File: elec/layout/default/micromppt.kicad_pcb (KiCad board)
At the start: 2 copper layers, 29 x 28.5 mm, 19 parts, among them J1 ?, J2 ?, U1 ?, U2 ?, U3 ?, U4 ?, U5 ?

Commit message: pcb update and actions retry
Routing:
- net gnd: vias 9 -> 21
- added copper zone on F.Cu, net gnd
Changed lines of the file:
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@@
 			(outputformat 1)
 			(mirror no)
-			(drillshape 1)
+			(drillshape 0)
 			(scaleselection 1)
-			(outputdirectory "")
+			(outputdirectory "../../../gerbers/")
 		)
 	)
@@
 	)
 	(gr_line
-		(start 87 39.2)
-		(end 72 39.2)
+		(start 65 67.75)
+		(end 94 67.75)
 		(stroke
 			(width 0.2)
@@
 	)
 	(gr_line
-		(start 65 67.75)
-		(end 94 67.75)
+		(start 87 39.2)
+		(end 72 39.2)
 		(stroke
 			(width 0.2)
@@
 	)
 	(segment
-		(start 86.1425 45.12)
-		(end 85.4 45.12)
-		(width 0.3048)
-		(layer "F.Cu")
-		(net 2)
-	)
-	(segment
 		(start 85.6 43.6)
 		(end 82.3 40.3)
@@
 	)
 	(segment
-		(start 85.6 44.92)
+		(start 85.6 44.5775)
 		(end 85.6 43.6)
 		(width 0.3048)
@@
 	)
 	(segment
+		(start 81.1525 44.25)
+		(end 80.2825 45.12)
+		(width 0.3048)
+		(layer "F.Cu")
+		(net 2)
+	)
+	(segment
 		(start 82.3 40.3)
 		(end 78.25 40.3)
@@
 	)
 	(segment
-		(start 74.76 41.64)
-		(end 74.76 42)
+		(start 85.2725 44.25)
+		(end 81.1525 44.25)
 		(width 0.3048)
 		(layer "F.Cu")
@@
 	(segment
 		(start 86.1425 45.12)
-		(end 80.2825 45.12)
+		(end 85.2725 44.25)
 		(width 0.3048)
 		(layer "F.Cu")
@@
 	)
 	(segment
-		(start 85.4 45.12)
-		(end 85.6 44.92)
+		(start 74.76 41.64)
+		(end 74.76 42)
+		(width 0.3048)
+		(layer "F.Cu")
+		(net 2)
+	)
+	(segment
+		(start 86.1425 45.12)
+		(end 85.6 44.5775)
 		(width 0.3048)
 		(layer "F.Cu")
@@
 	)
 	(via
+		(at 68 45.25)
+		(size 0.8)
+		(drill 0.4)
+		(layers "F.Cu" "B.Cu")
+		(free yes)
+		(net 6)
+	)
+	(via
+		(at 76.75 47.5)
+		(size 0.8)
+		(drill 0.4)
+		(layers "F.Cu" "B.Cu")
+		(free yes)
+		(net 6)
+	)
+	(via
+		(at 78.5 45.25)
+		(size 0.8)
+		(drill 0.4)
+		(layers "F.Cu" "B.Cu")
+		(free yes)
+		(net 6)
+	)
+	(via
 		(at 76.55 51)
 		(size 0.8)
@@
 	)
 	(via
+		(at 87.75 50.75)
+		(size 0.8)
+		(drill 0.4)
+		(layers "F.Cu" "B.Cu")
+		(free yes)
+		(net 6)
+	)
+	(via
+		(at 81.75 43.5)
+		(size 0.8)
+		(drill 0.4)
+		(layers "F.Cu" "B.Cu")
+		(free yes)
+		(net 6)
+	)
+	(via
 		(at 81.9 57.6)
 		(size 0.8)
@@
 	)
 	(via
+		(at 77.5 51.5)
+		(size 0.8)
+		(drill 0.4)
+		(layers "F.Cu" "B.Cu")
+		(free yes)
+		(net 6)
+	)
+	(via
+		(at 68 48.75)
+		(size 0.8)
+		(drill 0.4)
+		(layers "F.Cu" "B.Cu")
+		(free yes)
+		(net 6)
+	)
+	(via
+		(at 68 50.5)
+		(size 0.8)
+		(drill 0.4)
+		(layers "F.Cu" "B.Cu")
+		(free yes)
+		(net 6)
+	)
+	(via
+		(at 86 50.75)
+		(size 0.8)
+		(drill 0.4)
+		(layers "F.Cu" "B.Cu")
+		(free yes)
+		(net 6)
+	)
+	(via
 		(at 87.3 48)
 		(size 0.8)
@@
 	)
 	(via
+		(at 74.5 44)
+		(size 0.8)
+		(drill 0.4)
+		(layers "F.Cu" "B.Cu")
+		(free yes)
+		(net 6)
+	)
+	(via
 		(at 87 43.6)
 		(size 0.8)
@@
 	)
 	(via
+		(at 73.027028 44)
+		(size 0.8)
+		(drill 0.4)
+		(layers "F.Cu" "B.Cu")
+		(free yes)
+		(net 6)
+	)
+	(via
 		(at 68.5 52)
 		(size 0.8)
@@
 		(net 6)
 	)
+	(via
+		(at 68 47)
+		(size 0.8)
+		(drill 0.4)
+		(layers "F.Cu" "B.Cu")
+		(free yes)
+		(net 6)
+	)
 	(segment
 		(start 90.1125 45.4)
@@
 	)
 	(segment
-		(start 69.98 45.76)
-		(end 69.98 47.75)
+		(start 73.25 42)
+		(end 69.98 45.27)
 		(width 0.3048)
 		(layer "F.Cu")
@@
 	(segment
 		(start 73.74 42)
-		(end 69.98 45.76)
+		(end 73.25 42)
+		(width 0.3048)
+		(layer "F.Cu")
+		(net 12)
+	)
+	(segment
+		(start 69.98 45.27)
+		(end 69.98 47.75)
 		(width 0.3048)
 		(layer "F.Cu")
@@
 			)
 		)
+	)
+	(zone
+		(net 6)
+		(net_name "gnd")
+		(layer "F.Cu")
+		(hatch edge 0.5)
+		(connect_pads yes
+			(clearance 0.25)
+		)
+		(min_thickness 0.25)
+		(filled_areas_thickness no)
+		(fill yes
+			(thermal_gap 0.5)
+			(thermal_bridge_width 0.5)
+			(island_removal_mode 1)
+			(island_area_min 10)
+		)
+		(polygon
+			(pts
+				(xy 81.5 47.25) (xy 81.5 44.65) (xy 85 44.65) (xy 85 47.5) (xy 81.5 47.5)
+			)
+		)

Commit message: connected c3/r1
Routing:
- net vcc-2: track 22.1 -> 23.4 mm
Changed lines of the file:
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@@
+	)
+	(segment
+		(start 91.5 53)
+		(end 90.55 52.05)
+		(width 0.25)
+		(layer "F.Cu")
+		(net 13)
 	)
 	(segment

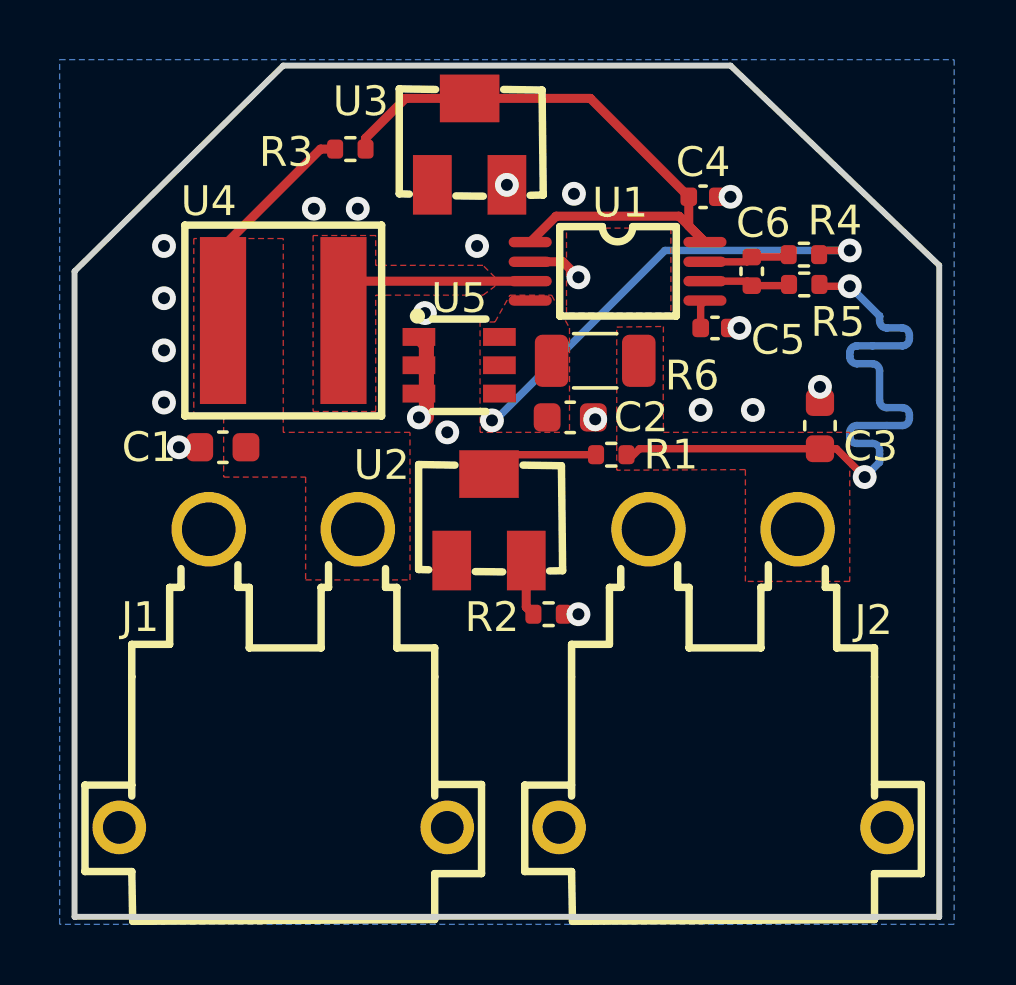
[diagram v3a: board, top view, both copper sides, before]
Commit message: fixed unconnected vout feedback pin
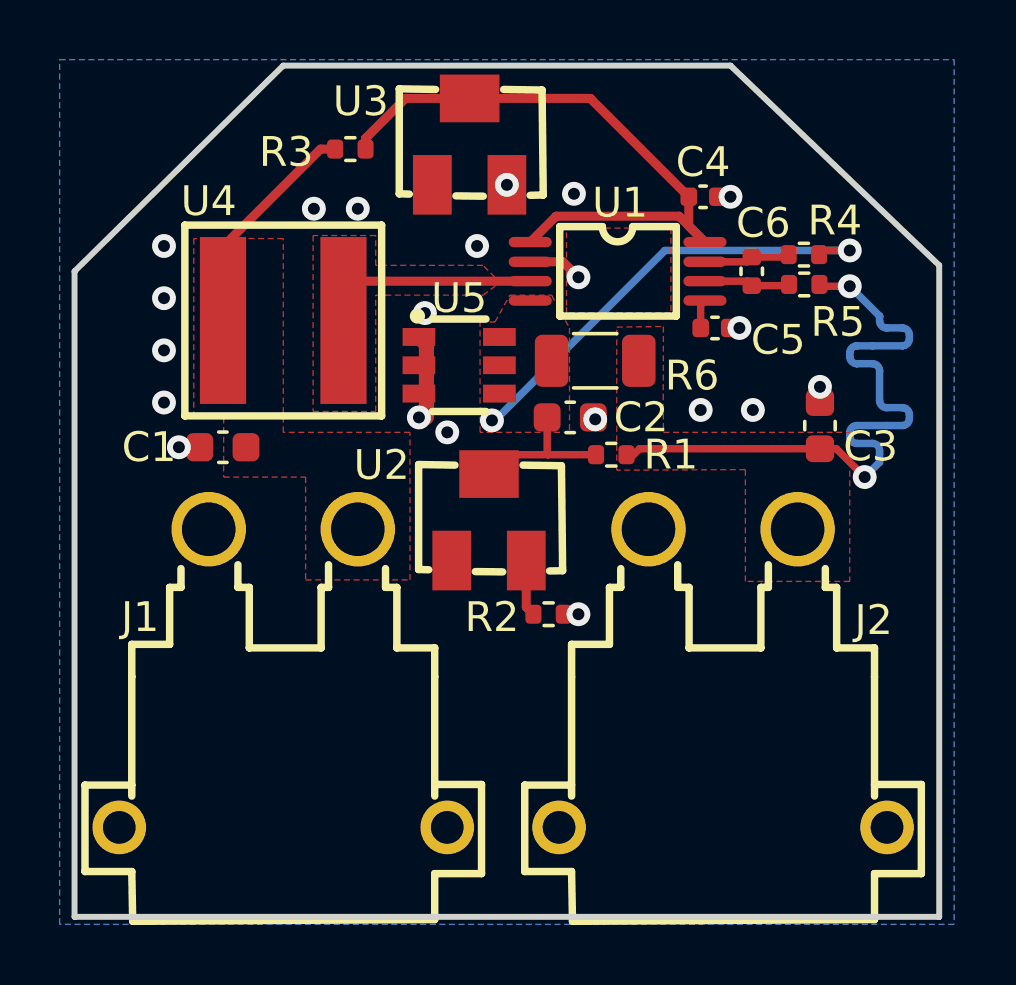
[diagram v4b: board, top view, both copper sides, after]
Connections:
- net mpp_minus_set renamed xshut
- R1 pad 2: p2 -> vout
- U2 pad 2: p2 -> vout
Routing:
- net vout: track 15.4 -> 21.1 mm
- net p2: track 4.42 -> 0.00 mm

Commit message: MICROMPPT V2
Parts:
- removed J1, J2: ?, lib:CONN-TH_XT30PW-M
- removed the U3 at (78.2, 41.8)
- moved R2 2.04 mm to (82.1, 56.0), turned to 90 degrees
- moved R3 1.10 mm to (73.7, 43.0)
- renumbered U4 to U3, U5 to U4
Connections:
- net VR2-p1 renamed p1
- R1 pad 2: vout -> vctrl
- U2 pad 2: vout -> vctrl
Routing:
- net vctrl: track 0.98 -> 13.0 mm, vias 0 -> 2
- net vcc-2: track 23.4 -> 13.7 mm, vias 2 -> 3
- net vout: track 21.1 -> 15.4 mm
- net xshut: track 21.4 -> 16.7 mm
- net vcc-1: track 7.59 -> 8.72 mm, vias 0 -> 1
- net gnd: vias 21 -> 23
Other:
- board size 29 x 28.5 mm -> 25.9 x 15.3 mm

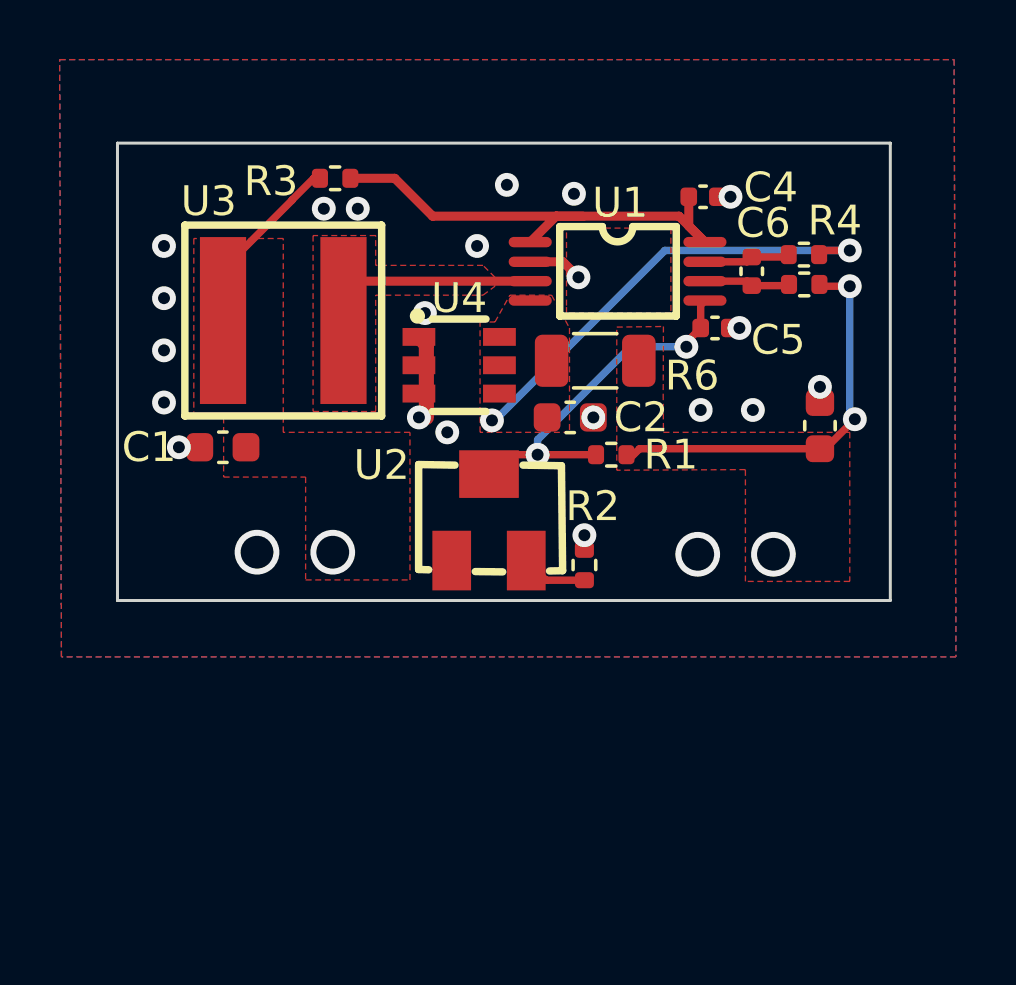
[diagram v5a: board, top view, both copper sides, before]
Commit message: built with ato v3, MICROMPPT V2 order
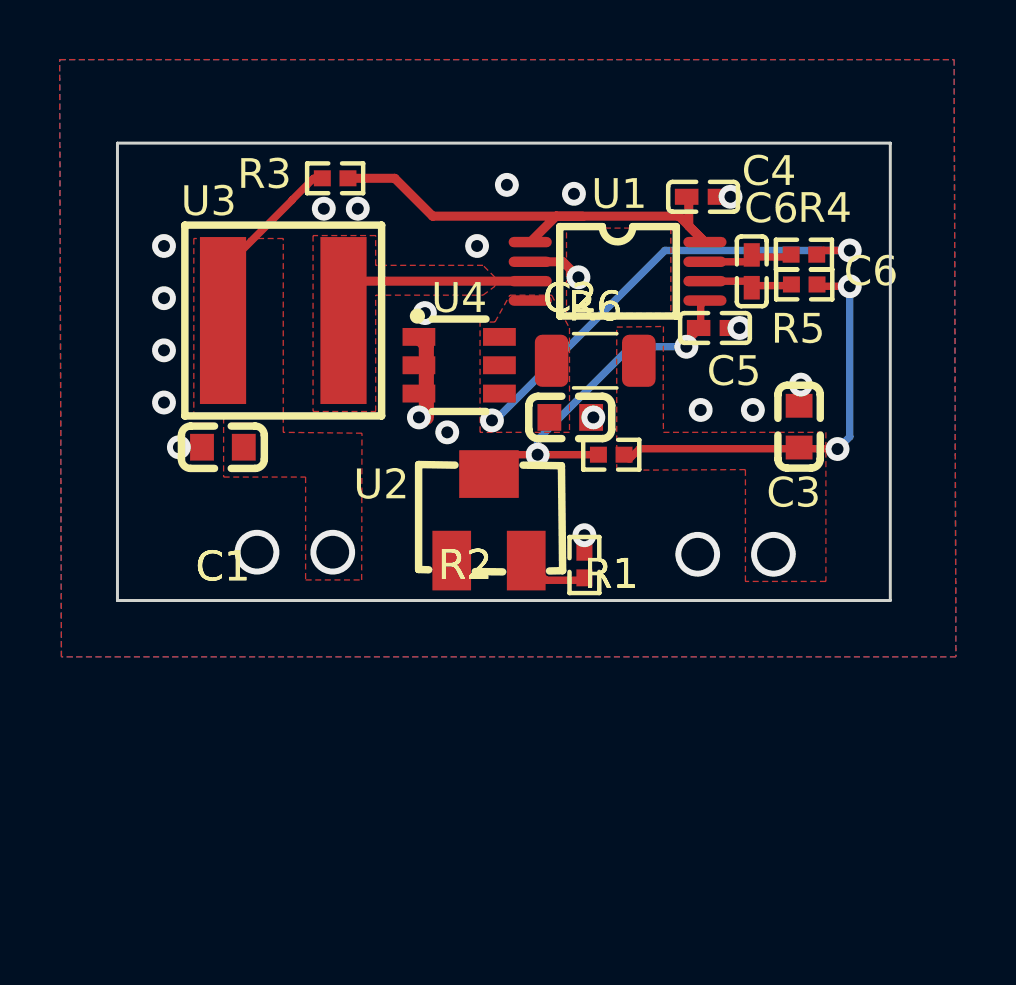
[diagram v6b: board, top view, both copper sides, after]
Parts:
- C1, C3: value 10V 10uF X5R ±10% 0603 Multilayer Ceramic Capacitors MLCC - SMD/SMT ROHS -> 10µF ±10% 10V X5R; footprint lib:C0603 -> atopile:C0603-bd72f6
- C2: value 16V 4.7uF X5R ±10% 0603 Multilayer Ceramic Capacitors MLCC - SMD/SMT ROHS -> 4.7µF ±10% 10V X5R; footprint lib:C0603 -> atopile:C0603-bd72f6
- C4: value 16V 100nF X7R ±10% 0402 Multilayer Ceramic Capacitors MLCC - SMD/SMT ROHS -> 100nF ±10% 16V X7R; footprint lib:C0402 -> atopile:C0402-b3ef17
- C5: value 50V 1nF X7R ±10% 0402 Multilayer Ceramic Capacitors MLCC - SMD/SMT ROHS -> 1nF ±10% 50V X7R; footprint lib:C0402 -> atopile:C0402-b3ef17
- C6: value 25V 1uF X5R ±10% 0402 Multilayer Ceramic Capacitors MLCC - SMD/SMT ROHS -> 1µF ±10% 25V X5R; footprint lib:C0402 -> atopile:C0402-b3ef17
- R1: value 62.5mW Thick Film Resistors 50V ±100ppm/℃ ±1% 1MΩ 0402 Chip Resistor - Surface Mount ROHS -> 1MΩ ±1% 62.5mW; footprint lib:R0402 -> atopile:R0402-56259e
- R2: value 62.5mW Thick Film Resistors 50V ±100ppm/℃ ±1% 300kΩ 0402 Chip Resistor - Surface Mount ROHS -> 300kΩ ±1% 62.5mW; footprint lib:R0402 -> atopile:R0402-56259e
- R3, R4, R5: value 62.5mW Thick Film Resistors 50V ±100ppm/℃ ±1% 1kΩ 0402 Chip Resistor - Surface Mount ROHS -> 1kΩ ±1% 62.5mW; footprint lib:R0402 -> atopile:R0402-56259e
- R6: value 1W 10mΩ ±70ppm/℃ ±1% 1206 Current Sense Resistors / Shunt Resistors ROHS -> 10mΩ ±1% 1W
- U1, U2, U3, U4: value ? -> (none)
- moved C3 0.70 mm to (89.3, 51.3)
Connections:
- net ictrl_minus renamed ICTRL_MINUS
- net ictrl_plus renamed ICTRL_PLUS
- net lx renamed LX
- net p1 renamed net
- net vcc-1 renamed hv-1
- net vcc-2 renamed hv
- net vctrl renamed VCTRL
- net vout renamed cathode
- net xshut renamed XSHUT

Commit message: v3 update
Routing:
- net gnd: vias 23 -> 25

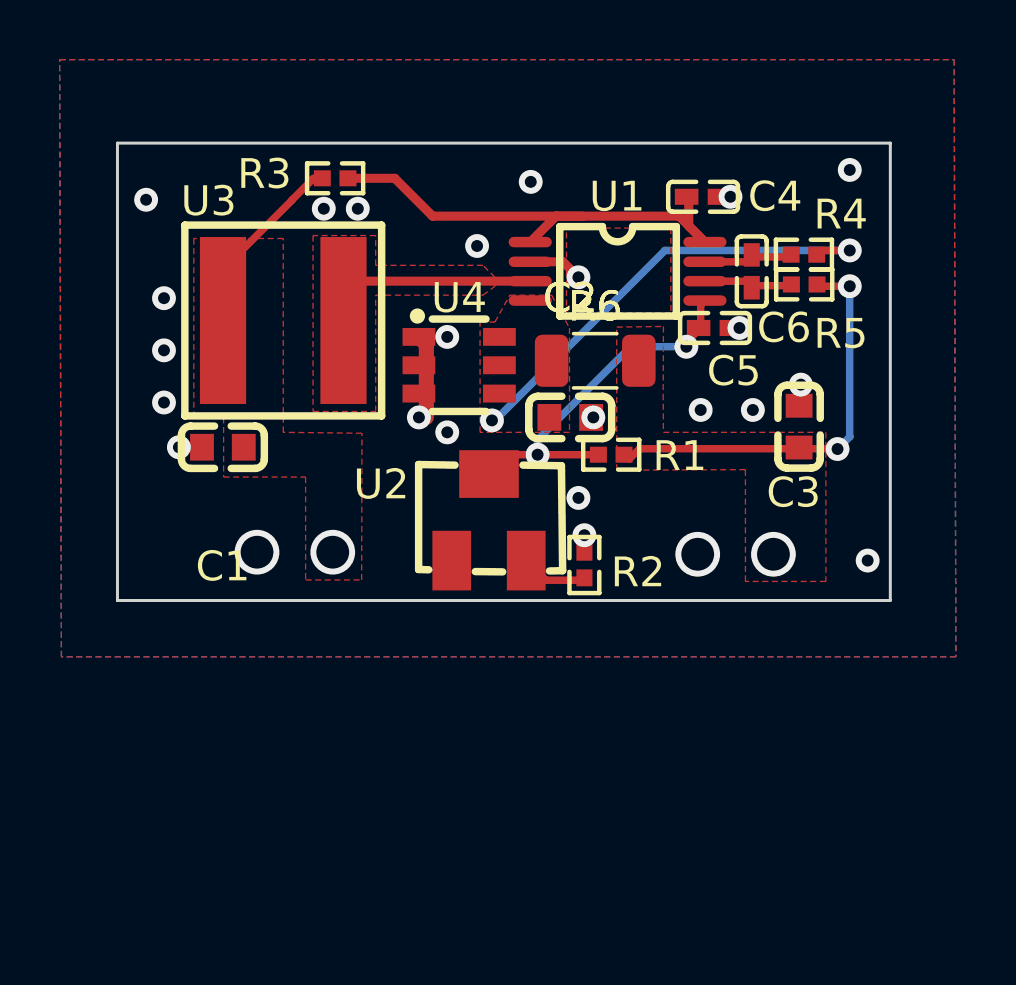
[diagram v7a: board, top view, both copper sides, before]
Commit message: Revert "v3 update"
This reverts commit 3d2f1a32cb7bdd8d1440f52d8c2b71f7bcce05a5.
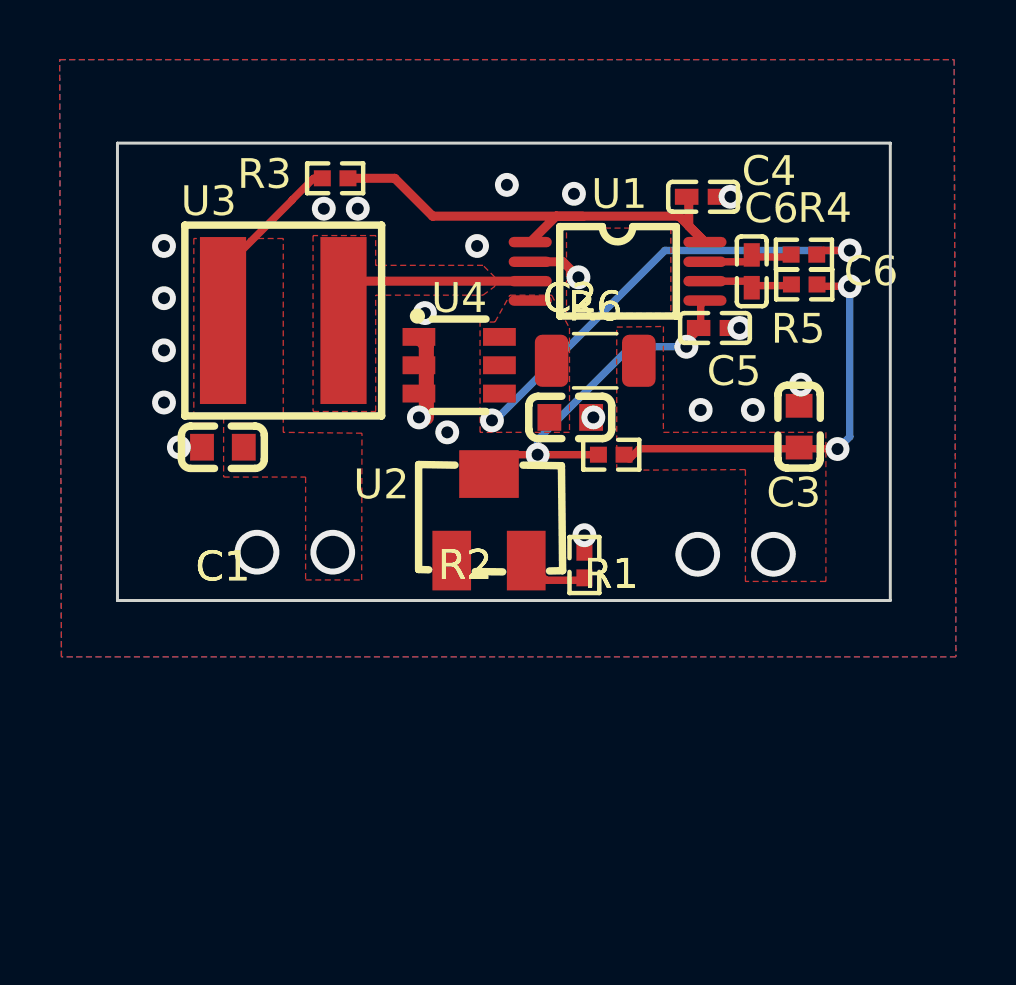
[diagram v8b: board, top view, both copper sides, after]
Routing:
- net gnd: vias 25 -> 23
